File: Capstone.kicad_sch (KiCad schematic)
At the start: 1 part, among them U1 XIAO-ESP32-S3-DIP

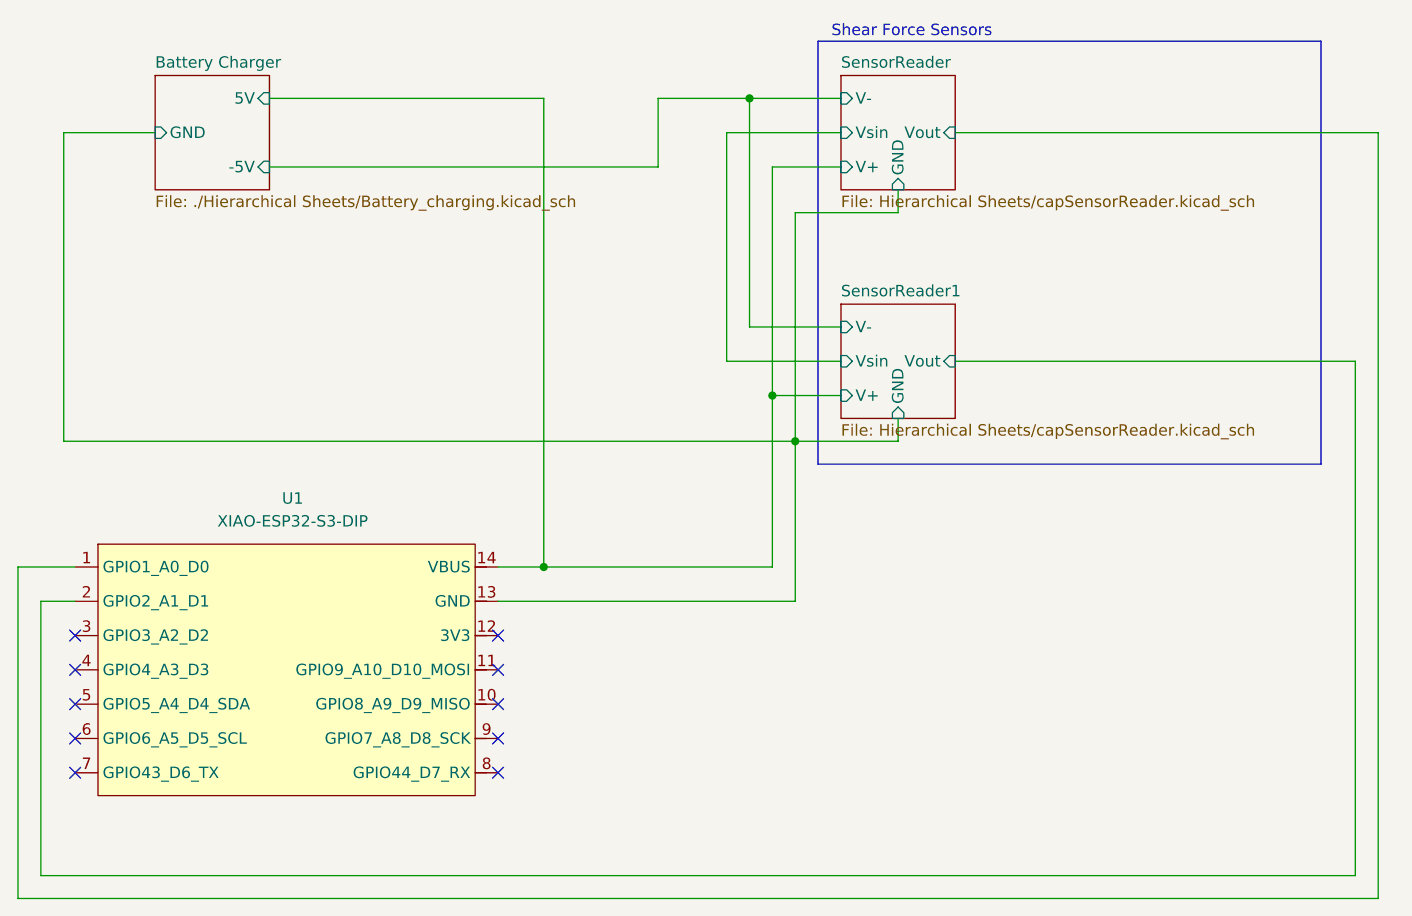
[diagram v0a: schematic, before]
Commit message: Remove extra ref sensor
each module had a reference sensor before, now have single ref sensor comparing to both sensors
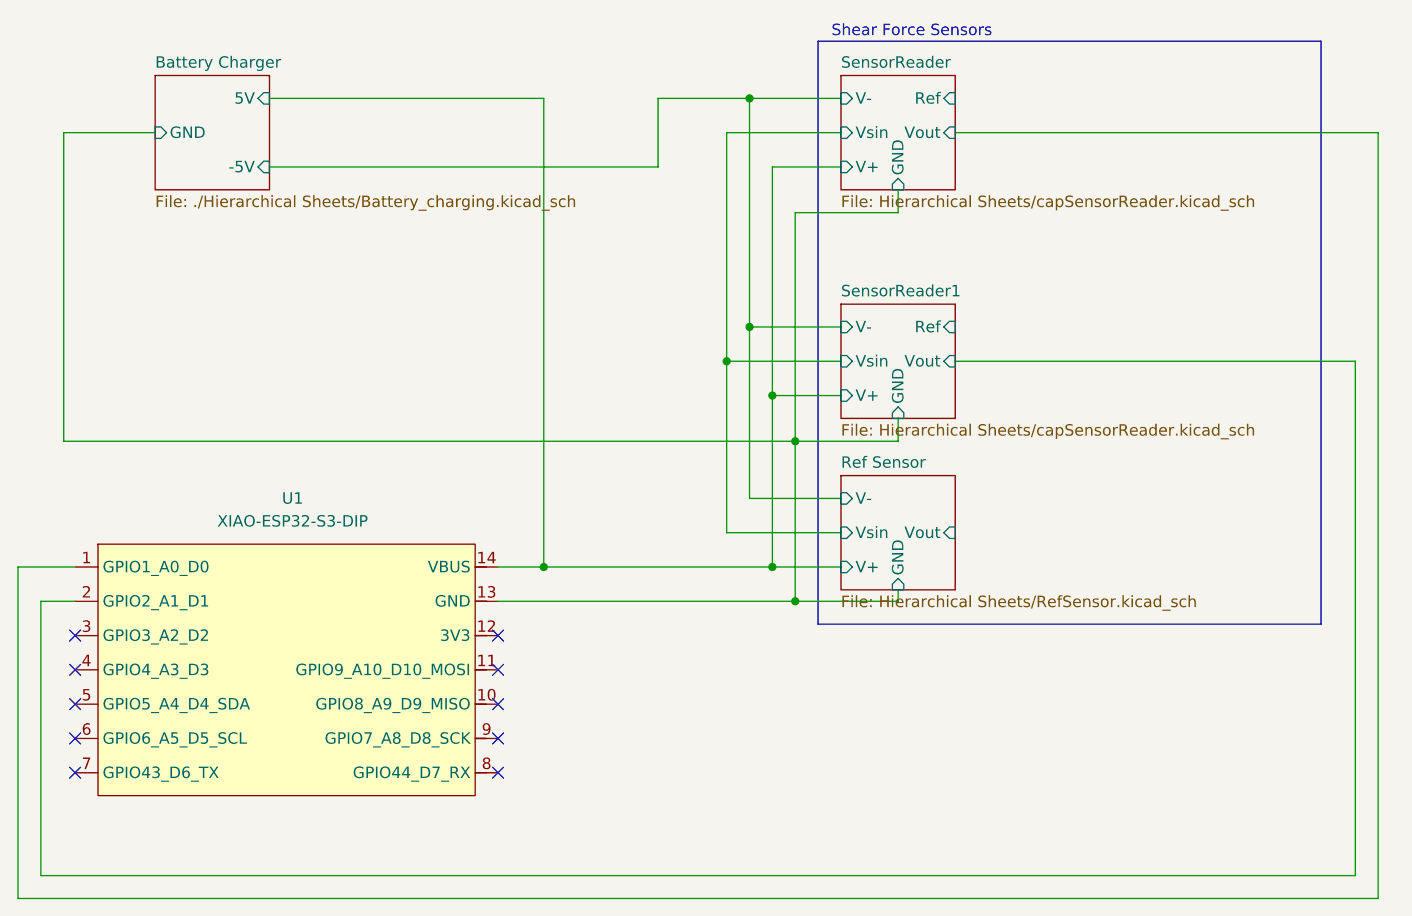
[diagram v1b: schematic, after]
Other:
- added sheet Ref Sensor (Hierarchical Sheets/RefSensor.kicad_sch)
- sheet SensorReader ports: added Ref; removed none
- sheet SensorReader1 ports: added Ref; removed none
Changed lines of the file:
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@@
 	(rectangle
 		(start 111.76 21.59)
-		(end 167.64 68.58)
+		(end 167.64 86.36)
 		(stroke
 			(width 0)
@@
 	)
 	(junction
+		(at 104.14 53.34)
+		(diameter 0)
+		(color 0 0 0 0)
+	)
+	(junction
 		(at 104.14 27.94)
 		(diameter 0)
@@
 	)
 	(junction
+		(at 109.22 83.82)
+		(diameter 0)
+		(color 0 0 0 0)
+	)
+	(junction
 		(at 81.28 80.01)
+		(diameter 0)
+		(color 0 0 0 0)
+	)
+	(junction
+		(at 106.68 80.01)
+		(diameter 0)
+		(color 0 0 0 0)
+	)
+	(junction
+		(at 101.6 57.15)
 		(diameter 0)
 		(color 0 0 0 0)
@@
 	(wire
 		(pts
+			(xy 104.14 72.39) (xy 104.14 53.34)
+		)
+		(stroke
+			(width 0)
+			(type default)
+		)
+	)
+	(wire
+		(pts
+			(xy 101.6 57.15) (xy 101.6 76.2)
+		)
+		(stroke
+			(width 0)
+			(type default)
+		)
+	)
+	(wire
+		(pts
+			(xy 106.68 80.01) (xy 114.3 80.01)
+		)
+		(stroke
+			(width 0)
+			(type default)
+		)
+	)
+	(wire
+		(pts
 			(xy 104.14 27.94) (xy 114.3 27.94)
 		)
@@
 	(wire
 		(pts
+			(xy 114.3 72.39) (xy 104.14 72.39)
+		)
+		(stroke
+			(width 0)
+			(type default)
+		)
+	)
+	(wire
+		(pts
 			(xy 101.6 31.75) (xy 101.6 57.15)
 		)
@@
 	(wire
 		(pts
+			(xy 120.65 83.82) (xy 120.65 82.55)
+		)
+		(stroke
+			(width 0)
+			(type default)
+		)
+	)
+	(wire
+		(pts
+			(xy 109.22 83.82) (xy 120.65 83.82)
+		)
+		(stroke
+			(width 0)
+			(type default)
+		)
+	)
+	(wire
+		(pts
 			(xy 81.28 80.01) (xy 106.68 80.01)
 		)
@@
 		(pts
 			(xy 171.45 57.15) (xy 171.45 114.3)
+		)
+		(stroke
+			(width 0)
+			(type default)
+		)
+	)
+	(wire
+		(pts
+			(xy 101.6 76.2) (xy 114.3 76.2)
 		)
 		(stroke
@@
 			)
 		)
+		(pin "Ref" input
+			(at 127 53.34 0)
+			(effects
+				(font
+					(size 1.27 1.27)
+				)
+				(justify right)
+			)
+		)
 		(instances
 			(project "Capstone"
@@
 			)
 		)
+		(pin "Ref" input
+			(at 127 27.94 0)
+			(effects
+				(font
+					(size 1.27 1.27)
+				)
+				(justify right)
+			)
+		)
 		(instances
 			(project "Capstone"
@@
 				)
 			)
+		)
+	)
+	(sheet
+		(at 114.3 69.85)
+		(size 12.7 12.7)
+		(exclude_from_sim no)
+		(in_bom yes)
+		(on_board yes)
+		(dnp no)
+		(fields_autoplaced yes)
+		(stroke
+			(width 0.1524)
+			(type solid)
+		)
+		(fill
+			(color 0 0 0 0.0000)
+		)
+		(property "Sheetname" "Ref Sensor"
+			(at 114.3 69.1384 0)
+			(effects
+				(font
+					(size 1.27 1.27)
+				)
+				(justify left bottom)
+			)
+		)
+		(property "Sheetfile" "Hierarchical Sheets/RefSensor.kicad_sch"
+			(at 114.3 83.1346 0)
+			(effects
+				(font
+					(size 1.27 1.27)
+				)
+				(justify left top)
+			)
+		)
+		(pin "V+" input
+			(at 114.3 80.01 180)
+			(effects
+				(font
+					(size 1.27 1.27)
+				)
+				(justify left)
+			)
+		)
+		(pin "V-" input
+			(at 114.3 72.39 180)
+			(effects
+				(font
+					(size 1.27 1.27)
+				)
+				(justify left)
+			)
+		)
+		(pin "Vout" input
+			(at 127 76.2 0)
+			(effects
+				(font
+					(size 1.27 1.27)
+				)
+				(justify right)
+			)
+		)
+		(pin "Vsin" input
+			(at 114.3 76.2 180)
+			(effects
+				(font
+					(size 1.27 1.27)
+				)
+				(justify left)
+			)
+		)
+		(pin "GND" input
+			(at 120.65 82.55 270)
+			(effects
+				(font
+					(size 1.27 1.27)
+				)
+				(justify left)
+			)
+		)
+		(instances
+			(project "Capstone"
+				(path "/eb20fb8b-6e33-462b-9505-401dab49dd09"
+					(page "5")
+				)
+			)

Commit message: Revert "Remove extra ref sensor"
This reverts commit 7f0b0207ac24b991faee57c630f393e10dd69dda.
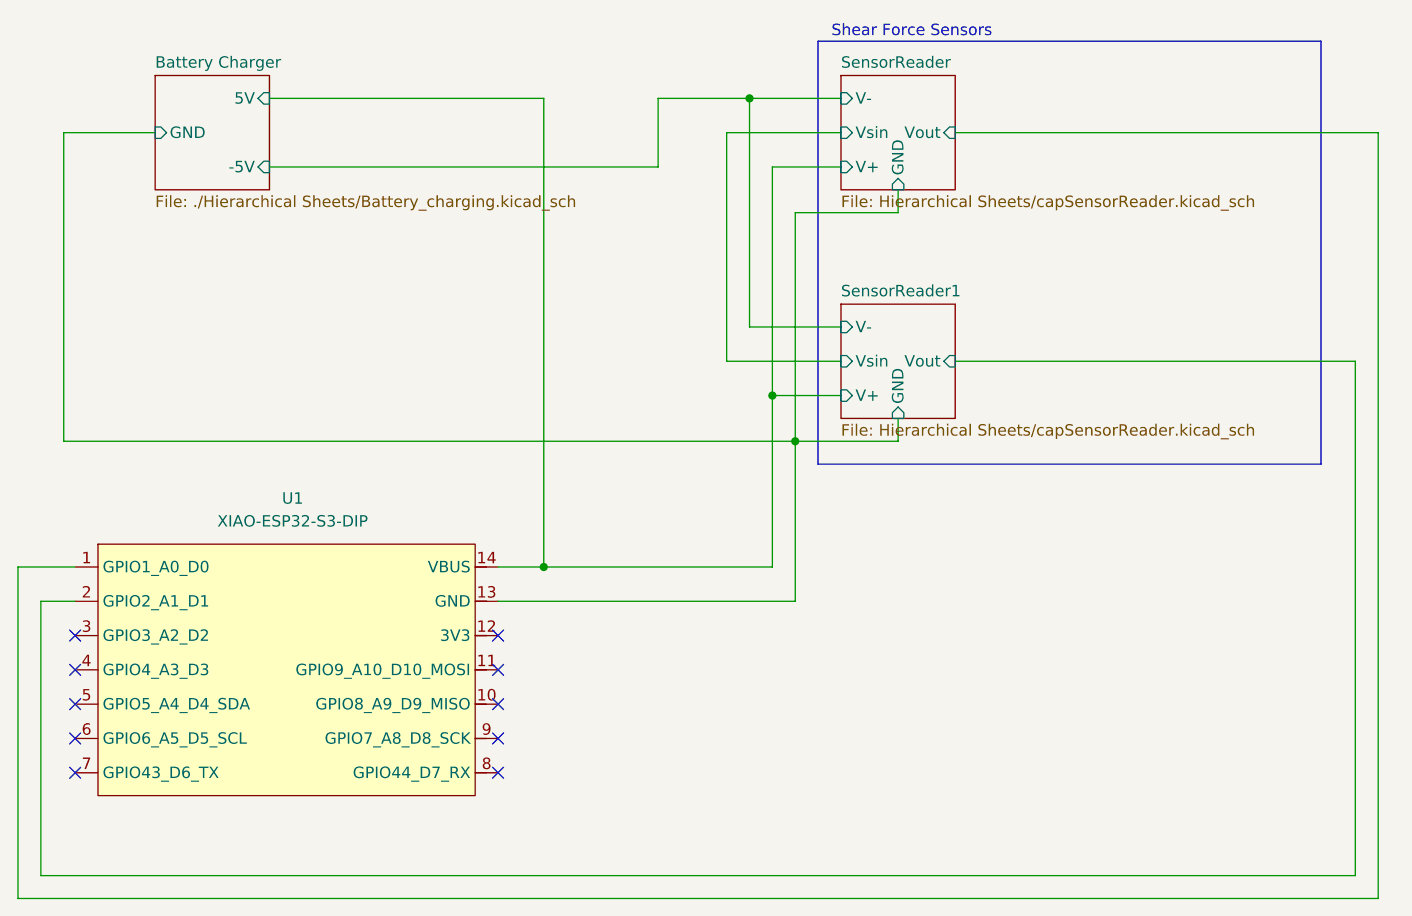
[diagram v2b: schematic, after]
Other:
- removed sheet Ref Sensor
- sheet SensorReader ports: added none; removed Ref
- sheet SensorReader1 ports: added none; removed Ref
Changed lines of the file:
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@@
 	(rectangle
 		(start 111.76 21.59)
-		(end 167.64 86.36)
+		(end 167.64 68.58)
 		(stroke
 			(width 0)
@@
 	)
 	(junction
-		(at 104.14 53.34)
-		(diameter 0)
-		(color 0 0 0 0)
-	)
-	(junction
 		(at 104.14 27.94)
 		(diameter 0)
@@
 	)
 	(junction
-		(at 109.22 83.82)
-		(diameter 0)
-		(color 0 0 0 0)
-	)
-	(junction
 		(at 81.28 80.01)
-		(diameter 0)
-		(color 0 0 0 0)
-	)
-	(junction
-		(at 106.68 80.01)
-		(diameter 0)
-		(color 0 0 0 0)
-	)
-	(junction
-		(at 101.6 57.15)
 		(diameter 0)
 		(color 0 0 0 0)
@@
 	(wire
 		(pts
-			(xy 104.14 72.39) (xy 104.14 53.34)
-		)
-		(stroke
-			(width 0)
-			(type default)
-		)
-	)
-	(wire
-		(pts
-			(xy 101.6 57.15) (xy 101.6 76.2)
-		)
-		(stroke
-			(width 0)
-			(type default)
-		)
-	)
-	(wire
-		(pts
-			(xy 106.68 80.01) (xy 114.3 80.01)
-		)
-		(stroke
-			(width 0)
-			(type default)
-		)
-	)
-	(wire
-		(pts
 			(xy 104.14 27.94) (xy 114.3 27.94)
 		)
@@
 	(wire
 		(pts
-			(xy 114.3 72.39) (xy 104.14 72.39)
-		)
-		(stroke
-			(width 0)
-			(type default)
-		)
-	)
-	(wire
-		(pts
 			(xy 101.6 31.75) (xy 101.6 57.15)
 		)
@@
 	(wire
 		(pts
-			(xy 120.65 83.82) (xy 120.65 82.55)
-		)
-		(stroke
-			(width 0)
-			(type default)
-		)
-	)
-	(wire
-		(pts
-			(xy 109.22 83.82) (xy 120.65 83.82)
-		)
-		(stroke
-			(width 0)
-			(type default)
-		)
-	)
-	(wire
-		(pts
 			(xy 81.28 80.01) (xy 106.68 80.01)
 		)
@@
 		(pts
 			(xy 171.45 57.15) (xy 171.45 114.3)
-		)
-		(stroke
-			(width 0)
-			(type default)
-		)
-	)
-	(wire
-		(pts
-			(xy 101.6 76.2) (xy 114.3 76.2)
 		)
 		(stroke
@@
 			)
 		)
-		(pin "Ref" input
-			(at 127 53.34 0)
-			(effects
-				(font
-					(size 1.27 1.27)
-				)
-				(justify right)
-			)
-		)
 		(instances
 			(project "Capstone"
@@
 			)
 		)
-		(pin "Ref" input
-			(at 127 27.94 0)
-			(effects
-				(font
-					(size 1.27 1.27)
-				)
-				(justify right)
-			)
-		)
 		(instances
 			(project "Capstone"
@@
 				)
 			)
-		)
-	)
-	(sheet
-		(at 114.3 69.85)
-		(size 12.7 12.7)
-		(exclude_from_sim no)
-		(in_bom yes)
-		(on_board yes)
-		(dnp no)
-		(fields_autoplaced yes)
-		(stroke
-			(width 0.1524)
-			(type solid)
-		)
-		(fill
-			(color 0 0 0 0.0000)
-		)
-		(property "Sheetname" "Ref Sensor"
-			(at 114.3 69.1384 0)
-			(effects
-				(font
-					(size 1.27 1.27)
-				)
-				(justify left bottom)
-			)
-		)
-		(property "Sheetfile" "Hierarchical Sheets/RefSensor.kicad_sch"
-			(at 114.3 83.1346 0)
-			(effects
-				(font
-					(size 1.27 1.27)
-				)
-				(justify left top)
-			)
-		)
-		(pin "V+" input
-			(at 114.3 80.01 180)
-			(effects
-				(font
-					(size 1.27 1.27)
-				)
-				(justify left)
-			)
-		)
-		(pin "V-" input
-			(at 114.3 72.39 180)
-			(effects
-				(font
-					(size 1.27 1.27)
-				)
-				(justify left)
-			)
-		)
-		(pin "Vout" input
-			(at 127 76.2 0)
-			(effects
-				(font
-					(size 1.27 1.27)
-				)
-				(justify right)
-			)
-		)
-		(pin "Vsin" input
-			(at 114.3 76.2 180)
-			(effects
-				(font
-					(size 1.27 1.27)
-				)
-				(justify left)
-			)
-		)
-		(pin "GND" input
-			(at 120.65 82.55 270)
-			(effects
-				(font
-					(size 1.27 1.27)
-				)
-				(justify left)
-			)
-		)
-		(instances
-			(project "Capstone"
-				(path "/eb20fb8b-6e33-462b-9505-401dab49dd09"
-					(page "5")
-				)
-			)
